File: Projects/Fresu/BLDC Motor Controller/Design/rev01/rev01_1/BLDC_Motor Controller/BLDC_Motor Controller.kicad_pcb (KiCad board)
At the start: 2 copper layers, 65 x 56 mm, 4 parts

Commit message: Update 14
Added 4 mounting holes, imported all components into PCB project, created board outline
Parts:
- removed MH1, MH2, MH3, MH4: MountingHole_2.7mm_M2.5, MountingHole:MountingHole_2.7mm_M2.5
- added C1: C, Capacitor_SMD:C_0603_1608Metric, F.Cu at (444.5, 121.0)
- added C10: 2u2, Capacitor_SMD:C_0603_1608Metric, F.Cu at (448.5, 128.5)
- added C11: 100n, Capacitor_SMD:C_0603_1608Metric, F.Cu at (448.5, 131.0)
- added C12: 1u, Capacitor_SMD:C_0603_1608Metric, F.Cu at (448.5, 133.5)
- added C13: 10p, Capacitor_SMD:C_0603_1608Metric, F.Cu at (452.5, 121.0)
- added C14: 10p, Capacitor_SMD:C_0603_1608Metric, F.Cu at (452.5, 123.5)
- added C15: 100n, Capacitor_SMD:C_0603_1608Metric, F.Cu at (452.5, 126.0)
- added C16: 100n, Capacitor_SMD:C_0603_1608Metric, F.Cu at (452.5, 128.5)
- added C17: 100nF, Capacitor_SMD:C_0603_1608Metric, F.Cu at (452.5, 131.0)
- added C18: 2u2, Capacitor_SMD:C_0603_1608Metric, F.Cu at (497.8, 100.1)
- added C19: 2u2, Capacitor_SMD:C_0603_1608Metric, F.Cu at (497.8, 102.6)
- added C2: 100nF, Capacitor_SMD:C_0603_1608Metric, F.Cu at (444.5, 123.5)
- added C20: 2u2, Capacitor_SMD:C_0603_1608Metric, F.Cu at (497.8, 105.1)
- added C21: 2u2, Capacitor_SMD:C_0603_1608Metric, F.Cu at (497.8, 107.6)
- added C22: 10n, Capacitor_SMD:C_0603_1608Metric, F.Cu at (497.8, 110.1)
- added C23: 120p, Capacitor_SMD:C_0603_1608Metric, F.Cu at (497.8, 112.6)
- added C24: 22n, Capacitor_SMD:C_0603_1608Metric, F.Cu at (501.8, 100.1)
- added C25: 2u2, Capacitor_SMD:C_0603_1608Metric, F.Cu at (501.8, 102.6)
- added C26: 100n, Capacitor_SMD:C_0603_1608Metric, F.Cu at (501.8, 105.1)
- added C27: 100n, Capacitor_SMD:C_0603_1608Metric, F.Cu at (501.8, 107.6)
- added C28: 100n, Capacitor_SMD:C_0603_1608Metric, F.Cu at (501.8, 110.1)
- added C29: 10n, Capacitor_SMD:C_0603_1608Metric, F.Cu at (501.8, 112.6)
- added C3: 100nF, Capacitor_SMD:C_0603_1608Metric, F.Cu at (444.5, 126.0)
- added C30: 10u, Capacitor_SMD:C_0603_1608Metric, F.Cu at (505.8, 100.1)
- added C31: 100n, Capacitor_SMD:C_0603_1608Metric, F.Cu at (505.8, 102.6)
- added C32: 10u, Capacitor_SMD:C_0603_1608Metric, F.Cu at (505.8, 105.1)
- added C33: 10u, Capacitor_SMD:C_0603_1608Metric, F.Cu at (505.8, 107.6)
- added C34: 100n, Capacitor_SMD:C_0603_1608Metric, F.Cu at (505.8, 110.1)
- added C35: 10u, Capacitor_SMD:C_0603_1608Metric, F.Cu at (505.8, 112.6)
- added C36: 10u, Capacitor_SMD:C_0603_1608Metric, F.Cu at (509.8, 100.1)
- added C37: 100n, Capacitor_SMD:C_0603_1608Metric, F.Cu at (509.8, 102.6)
- added C38: 10u, Capacitor_SMD:C_0603_1608Metric, F.Cu at (509.8, 105.1)
- added C39: 10u, Capacitor_SMD:C_0603_1608Metric, F.Cu at (509.8, 107.6)
- added C4: 100nF, Capacitor_SMD:C_0603_1608Metric, F.Cu at (444.5, 128.5)
- added C40: 10u, Capacitor_SMD:C_0603_1608Metric, F.Cu at (509.8, 110.1)
- added C41: 10u, Capacitor_SMD:C_0603_1608Metric, F.Cu at (509.8, 112.6)
- added C42: 2N2, Capacitor_SMD:C_0603_1608Metric, F.Cu at (516.2, 56.3)
- added C43: 2N2, Capacitor_SMD:C_0603_1608Metric, F.Cu at (516.2, 58.8)
- added C44: 100n, Capacitor_SMD:C_0603_1608Metric, F.Cu at (487.1, 78.0)
- added C45: 51p, Capacitor_SMD:C_0603_1608Metric, F.Cu at (515.8, 113.5)
- added C46: 51p, Capacitor_SMD:C_0603_1608Metric, F.Cu at (515.8, 116.0)
- added C47: 2u2, Capacitor_SMD:C_0603_1608Metric, F.Cu at (515.8, 118.5)
- added C48: 4n7, Capacitor_SMD:C_0603_1608Metric, F.Cu at (487.1, 80.5)
- added C49: 4n7, Capacitor_SMD:C_0603_1608Metric, F.Cu at (487.1, 83.0)
- added C5: 100nF, Capacitor_SMD:C_0603_1608Metric, F.Cu at (444.5, 131.0)
- added C50: 100n, Capacitor_SMD:C_0603_1608Metric, F.Cu at (487.1, 85.5)
- added C51: 4n7, Capacitor_SMD:C_0603_1608Metric, F.Cu at (487.1, 88.0)
- added C52: 100n, Capacitor_SMD:C_0603_1608Metric, F.Cu at (487.1, 90.5)
- added C53: 4n7, Capacitor_SMD:C_0603_1608Metric, F.Cu at (487.1, 93.0)
- added C54: 100n, Capacitor_SMD:C_0603_1608Metric, F.Cu at (487.1, 95.6)
- added C55: 1u, Capacitor_SMD:C_0603_1608Metric, F.Cu at (526.3, 34.9)
- added C56: 1u, Capacitor_SMD:C_0603_1608Metric, F.Cu at (526.3, 37.4)
- added C57: 1u, Capacitor_SMD:C_0603_1608Metric, F.Cu at (526.3, 39.9)
- added C58: 1u, Capacitor_SMD:C_0603_1608Metric, F.Cu at (526.3, 42.4)
- added C59: LKMI2501K821MF, DF_ESC_Footprint_Library:CAP-TH_BD18.0-P7.50-D1.2-SIDE, F.Cu at (450.6, 38.5)
- added C6: 100nF, Capacitor_SMD:C_0603_1608Metric, F.Cu at (444.5, 133.5)
- added C61: 100n, Capacitor_SMD:C_0603_1608Metric, F.Cu at (480.3, 79.7)
- added C62: 100n, Capacitor_SMD:C_0603_1608Metric, F.Cu at (480.3, 82.2)
- added C63: LKMI2501K821MF, DF_ESC_Footprint_Library:CAP-TH_BD18.0-P7.50-D1.2-SIDE, F.Cu at (471.0, 38.5)
- added C7: 100nF, Capacitor_SMD:C_0603_1608Metric, F.Cu at (448.5, 121.0)
- added C8: 100nF, Capacitor_SMD:C_0603_1608Metric, F.Cu at (448.5, 123.5)
- added C9: 2u2, Capacitor_SMD:C_0603_1608Metric, F.Cu at (448.5, 126.0)
- added CN1: XT60PW-M, DF_ESC_Footprint_Library:CONN-TH_XT60PW-M, F.Cu at (452.2, 83.5)
- added D1: LED_G, LED_SMD:LED_1206_3216Metric, F.Cu at (472.7, 95.5)
- added D10: BAT60A, Diode_SMD:D_SOD-323, F.Cu at (536.2, 48.4)
- added D11: ESDCAN24-2BLY, Package_TO_SOT_SMD:TSOT-23, F.Cu at (532.0, 120.9)
- added D12: LED_G, LED_SMD:LED_1206_3216Metric, F.Cu at (531.2, 47.0)
- added D13: SMAJ60CA, Diode_SMD:D_SMA, F.Cu at (465.9, 89.4)
- added D14: LED_G, LED_SMD:LED_1206_3216Metric, F.Cu at (476.8, 76.8)
- added D2: LED_R, LED_SMD:LED_1206_3216Metric, F.Cu at (472.7, 98.9)
- added D3: BAT60A, Diode_SMD:D_SOD-323, F.Cu at (477.6, 95.3)
- added D4: BAT60A, Diode_SMD:D_SOD-323, F.Cu at (477.6, 98.3)
- added D5: SD05_SOD323, Diode_SMD:D_SOD-323, F.Cu at (477.6, 101.2)
- added D6: LED_G, LED_SMD:LED_1206_3216Metric, F.Cu at (472.7, 102.3)
- added D7: PMEG6020ELR, Diode_SMD:Nexperia_CFP3_SOD-123W, F.Cu at (498.6, 125.5)
- added D8: BAT60A, Diode_SMD:D_SOD-323, F.Cu at (503.5, 125.4)
- added D9: LED_G, LED_SMD:LED_1206_3216Metric, F.Cu at (531.2, 43.6)
- added FB1: FerriteBead, Inductor_SMD:L_0603_1608Metric_Pad1.05x0.95mm_HandSolder, F.Cu at (471.1, 121.0)
- added FL1: 744227S, DF_ESC_Footprint_Library:FILTER-SMD_4P-L9.2-W6.0-P2.54-TL, F.Cu at (523.9, 116.0)
- added H1: MountingHole_Pad, MountingHole:MountingHole_3.2mm_M3_Pad_Via, F.Cu at (165.4, 104.2)
- added H2: MountingHole_Pad, MountingHole:MountingHole_3.2mm_M3_Pad_Via, F.Cu at (165.4, 169.2)
- added H3: MountingHole_Pad, MountingHole:MountingHole_3.2mm_M3_Pad_Via, F.Cu at (255.4, 104.4)
- added H5: MountingHole_Pad, MountingHole:MountingHole_3.2mm_M3_Pad_Via, F.Cu at (255.2, 169.2)
- added J1: Conn_01x06, DF_ESC_Footprint_Library:CONN-SMD_S6B-XH-SM4-TB-LF-SN, F.Cu at (453.9, 114.1)
- added J10: XH-2PWBPZ, DF_ESC_Footprint_Library:CONN-SMD_XH-2PWBPZ, F.Cu at (467.9, 80.3)
- added J2: Conn_01x03, DF_ESC_Footprint_Library:CONN-SMD_XH-3AWB, F.Cu at (472.1, 111.6)
- added J3: Conn_01x08, DF_ESC_Footprint_Library:CONN-SMD_8P-P2.50_HX25003-8AWB, F.Cu at (456.2, 101.1)
- added J4: 7461084, 7461084:WE_7461084, F.Cu at (499.3, 39.4)
- added J5: 7461084, 7461084:WE_7461084, F.Cu at (499.3, 51.0)
- added J6: 7461084, 7461084:WE_7461084, F.Cu at (499.3, 62.5)
- added J7: TYPE-C-31-M-12, DF_ESC_Footprint_Library:USB-C_SMD-TYPE-C-31-M-12, F.Cu at (528.1, 81.7)
- added J8: Conn_01x06, DF_ESC_Footprint_Library:CONN-SMD_S6B-XH-SM4-TB-LF-SN, F.Cu at (504.9, 84.6)
- added L1: 22u, DF_ESC_Footprint_Library:IND-SMD_L7.8-W7.8_SDR0805, F.Cu at (490.5, 119.2)
- added NT1: NetTie_2, DF_ESC_Footprint_Library:NetTie_SMD_Pad_0.2mm, F.Cu at (507.2, 124.9)
- added NT2: NetTie_2, NetTie:NetTie-2_SMD_Pad0.5mm, F.Cu at (519.4, 55.8)
- added NT3: NetTie_2, DF_ESC_Footprint_Library:NetTie_SMD_Pad_3.00mm, F.Cu at (506.6, 57.6)
- added NT4: NetTie_2, NetTie:NetTie-2_SMD_Pad0.5mm, F.Cu at (519.4, 57.3)
- added NT5: NetTie_2, DF_ESC_Footprint_Library:NetTie_SMD_Pad_3.00mm, F.Cu at (509.6, 57.6)
- added NT6: NetTie_2, NetTie:NetTie-2_SMD_Pad0.5mm, F.Cu at (519.4, 58.8)
- added NT7: NetTie_2, DF_ESC_Footprint_Library:NetTie_SMD_Pad_3.00mm, F.Cu at (512.7, 57.6)
- added Q1: HSBA15810C, Package_DFN_QFN:PQFN-8-EP_6x5mm_P1.27mm_Generic, F.Cu at (489.2, 37.1)
- added Q2: HSBA15810C, Package_DFN_QFN:PQFN-8-EP_6x5mm_P1.27mm_Generic, F.Cu at (489.2, 43.9)
- added Q3: HSBA15810C, Package_DFN_QFN:PQFN-8-EP_6x5mm_P1.27mm_Generic, F.Cu at (489.2, 50.8)
- added Q4: HSBA15810C, Package_DFN_QFN:PQFN-8-EP_6x5mm_P1.27mm_Generic, F.Cu at (489.2, 57.6)
- added Q5: HSBA15810C, Package_DFN_QFN:PQFN-8-EP_6x5mm_P1.27mm_Generic, F.Cu at (489.2, 64.5)
- added Q6: HSBA15810C, Package_DFN_QFN:PQFN-8-EP_6x5mm_P1.27mm_Generic, F.Cu at (489.2, 71.3)
- added R1: 100R, Resistor_SMD:R_0603_1608Metric_Pad0.98x0.95mm_HandSolder, F.Cu at (471.1, 123.5)
- added R10: 2k2, Resistor_SMD:R_0603_1608Metric_Pad0.98x0.95mm_HandSolder, F.Cu at (479.8, 121.0)
- added R11: 16k, Resistor_SMD:R_0603_1608Metric_Pad0.98x0.95mm_HandSolder, F.Cu at (498.0, 115.1)
- added R12: 10k, Resistor_SMD:R_0603_1608Metric_Pad0.98x0.95mm_HandSolder, F.Cu at (498.0, 117.6)
- added R13: 205K, Resistor_SMD:R_0603_1608Metric_Pad0.98x0.95mm_HandSolder, F.Cu at (498.0, 120.2)
- added R14: 1M, Resistor_SMD:R_0603_1608Metric_Pad0.98x0.95mm_HandSolder, F.Cu at (498.0, 122.7)
- added R15: 39k, Resistor_SMD:R_0603_1608Metric_Pad0.98x0.95mm_HandSolder, F.Cu at (502.3, 115.1)
- added R16: 2K2, Resistor_SMD:R_0603_1608Metric_Pad0.98x0.95mm_HandSolder, F.Cu at (502.3, 117.6)
- added R17: 18K, Resistor_SMD:R_0603_1608Metric_Pad0.98x0.95mm_HandSolder, F.Cu at (502.3, 120.2)
- added R18: 3K3, Resistor_SMD:R_0603_1608Metric_Pad0.98x0.95mm_HandSolder, F.Cu at (502.3, 122.7)
- added R19: 39k, Resistor_SMD:R_0603_1608Metric_Pad0.98x0.95mm_HandSolder, F.Cu at (506.7, 115.1)
- added R2: 0R, Resistor_SMD:R_0603_1608Metric_Pad0.98x0.95mm_HandSolder, F.Cu at (471.1, 126.0)
- added R20: 2K2, Resistor_SMD:R_0603_1608Metric_Pad0.98x0.95mm_HandSolder, F.Cu at (506.7, 117.6)
- added R21: 39k, Resistor_SMD:R_0603_1608Metric_Pad0.98x0.95mm_HandSolder, F.Cu at (506.7, 120.2)
- added R22: 2K2, Resistor_SMD:R_0603_1608Metric_Pad0.98x0.95mm_HandSolder, F.Cu at (506.7, 122.7)
- added R23: 4R7, Resistor_SMD:R_0603_1608Metric_Pad0.98x0.95mm_HandSolder, F.Cu at (507.2, 43.7)
- added R24: 4R7, Resistor_SMD:R_0603_1608Metric_Pad0.98x0.95mm_HandSolder, F.Cu at (507.2, 46.2)
- added R25: 39K, Resistor_SMD:R_0603_1608Metric_Pad0.98x0.95mm_HandSolder, F.Cu at (507.2, 48.8)
- added R26: 4R7, Resistor_SMD:R_0603_1608Metric_Pad0.98x0.95mm_HandSolder, F.Cu at (507.2, 51.3)
- added R27: 4R7, Resistor_SMD:R_0603_1608Metric_Pad0.98x0.95mm_HandSolder, F.Cu at (507.2, 53.8)
- added R28: 39K, Resistor_SMD:R_0603_1608Metric_Pad0.98x0.95mm_HandSolder, F.Cu at (511.6, 43.7)
- added R29: 0R001, DF_ESC_Footprint_Library:RES-SMD_L7.0-W6.7, F.Cu at (545.3, 61.8)
- added R29: 0R001, DF_ESC_Footprint_Library:RES-SMD_L7.0-W6.7, F.Cu at (509.4, 38.0)
- added R3: 0R, Resistor_SMD:R_0603_1608Metric_Pad0.98x0.95mm_HandSolder, F.Cu at (471.1, 128.5)
- added R30: 100R, Resistor_SMD:R_0603_1608Metric_Pad0.98x0.95mm_HandSolder, F.Cu at (511.6, 46.2)
- added R31: 100R, Resistor_SMD:R_0603_1608Metric_Pad0.98x0.95mm_HandSolder, F.Cu at (511.6, 48.8)
- added R32: 4R7, Resistor_SMD:R_0603_1608Metric_Pad0.98x0.95mm_HandSolder, F.Cu at (511.6, 51.3)
- added R33: 4R7, Resistor_SMD:R_0603_1608Metric_Pad0.98x0.95mm_HandSolder, F.Cu at (511.6, 53.8)
- added R34: 100R, Resistor_SMD:R_0603_1608Metric_Pad0.98x0.95mm_HandSolder, F.Cu at (515.9, 43.7)
- added R35: 100R, Resistor_SMD:R_0603_1608Metric_Pad0.98x0.95mm_HandSolder, F.Cu at (515.9, 46.2)
- added R36: 39K, Resistor_SMD:R_0603_1608Metric_Pad0.98x0.95mm_HandSolder, F.Cu at (515.9, 48.8)
- added R37: 0R001, DF_ESC_Footprint_Library:RES-SMD_L7.0-W6.7, F.Cu at (518.0, 38.0)
- added R37: 0R, Resistor_SMD:R_0603_1608Metric_Pad0.98x0.95mm_HandSolder, F.Cu at (224.4, 126.7)
- added R38: 2k2, Resistor_SMD:R_0603_1608Metric_Pad0.98x0.95mm_HandSolder, F.Cu at (491.3, 78.0)
- added R39: 10R, Resistor_SMD:R_0603_1608Metric_Pad0.98x0.95mm_HandSolder, F.Cu at (535.6, 100.1)
- added R4: 1k, Resistor_SMD:R_0603_1608Metric_Pad0.98x0.95mm_HandSolder, F.Cu at (471.1, 131.0)
- added R40: 10R, Resistor_SMD:R_0603_1608Metric_Pad0.98x0.95mm_HandSolder, F.Cu at (535.6, 102.6)
- added R41: 120R, Resistor_SMD:R_0603_1608Metric_Pad0.98x0.95mm_HandSolder, F.Cu at (535.6, 105.1)
- added R42: 10K, Resistor_SMD:R_0603_1608Metric_Pad0.98x0.95mm_HandSolder, F.Cu at (535.6, 107.6)
- added R43: 10k, Resistor_SMD:R_0603_1608Metric_Pad0.98x0.95mm_HandSolder, F.Cu at (491.3, 80.5)
- added R44: 2k2, Resistor_SMD:R_0603_1608Metric_Pad0.98x0.95mm_HandSolder, F.Cu at (491.3, 83.0)
- added R45: 10k, Resistor_SMD:R_0603_1608Metric_Pad0.98x0.95mm_HandSolder, F.Cu at (491.3, 85.5)
- added R46: 2k2, Resistor_SMD:R_0603_1608Metric_Pad0.98x0.95mm_HandSolder, F.Cu at (491.3, 88.0)
- added R47: 10k, Resistor_SMD:R_0603_1608Metric_Pad0.98x0.95mm_HandSolder, F.Cu at (491.3, 90.5)
- added R48: 10k, Resistor_SMD:R_0603_1608Metric_Pad0.98x0.95mm_HandSolder, F.Cu at (491.3, 93.0)
- added R49: 0R, Resistor_SMD:R_0603_1608Metric_Pad0.98x0.95mm_HandSolder, F.Cu at (491.3, 95.6)
- added R5: 1k, Resistor_SMD:R_0603_1608Metric_Pad0.98x0.95mm_HandSolder, F.Cu at (475.5, 121.0)
- added R50: 1k, Resistor_SMD:R_0603_1608Metric_Pad0.98x0.95mm_HandSolder, F.Cu at (536.2, 43.1)
- added R51: 1k, Resistor_SMD:R_0603_1608Metric_Pad0.98x0.95mm_HandSolder, F.Cu at (536.2, 45.6)
- added R52: 39k, Resistor_SMD:R_0603_1608Metric_Pad0.98x0.95mm_HandSolder, F.Cu at (476.1, 79.7)
- added R53: 2k2, Resistor_SMD:R_0603_1608Metric_Pad0.98x0.95mm_HandSolder, F.Cu at (476.1, 82.2)
- added R54: 39k, Resistor_SMD:R_0603_1608Metric_Pad0.98x0.95mm_HandSolder, F.Cu at (476.1, 84.8)
- added R55: 2k2, Resistor_SMD:R_0603_1608Metric_Pad0.98x0.95mm_HandSolder, F.Cu at (476.1, 87.3)
- added R56: 2k2, Resistor_SMD:R_0603_1608Metric_Pad0.98x0.95mm_HandSolder, F.Cu at (479.8, 123.5)
- added R57: 0R, Resistor_SMD:R_0603_1608Metric_Pad0.98x0.95mm_HandSolder, F.Cu at (520.5, 78.0)
- added R58: 0R, Resistor_SMD:R_0603_1608Metric_Pad0.98x0.95mm_HandSolder, F.Cu at (520.5, 80.5)
- added R59: 22R, Resistor_SMD:R_0603_1608Metric_Pad0.98x0.95mm_HandSolder, F.Cu at (520.5, 83.0)
- added R6: 1k, Resistor_SMD:R_0603_1608Metric_Pad0.98x0.95mm_HandSolder, F.Cu at (475.5, 123.5)
- added R60: 22R, Resistor_SMD:R_0603_1608Metric_Pad0.98x0.95mm_HandSolder, F.Cu at (520.5, 85.5)
- added R61: 5K1, Resistor_SMD:R_0603_1608Metric_Pad0.98x0.95mm_HandSolder, F.Cu at (520.5, 88.0)
- added R62: 5K1, Resistor_SMD:R_0603_1608Metric_Pad0.98x0.95mm_HandSolder, F.Cu at (520.5, 90.5)
- added R63: 0R, Resistor_SMD:R_0603_1608Metric_Pad0.98x0.95mm_HandSolder, F.Cu at (520.5, 93.0)
- added R64: 0R001, DF_ESC_Footprint_Library:RES-SMD_L7.0-W6.7, F.Cu at (553.9, 61.8)
- added R65: 0R, Resistor_SMD:R_0603_1608Metric_Pad0.98x0.95mm_HandSolder, F.Cu at (224.4, 129.2)
- added R66: 0R, Resistor_SMD:R_0603_1608Metric_Pad0.98x0.95mm_HandSolder, F.Cu at (224.4, 131.7)
- added R67: 0R, Resistor_SMD:R_0603_1608Metric_Pad0.98x0.95mm_HandSolder, F.Cu at (224.4, 134.2)
- added R7: 2k2, Resistor_SMD:R_0603_1608Metric_Pad0.98x0.95mm_HandSolder, F.Cu at (475.5, 126.0)
- added R8: 2k2, Resistor_SMD:R_0603_1608Metric_Pad0.98x0.95mm_HandSolder, F.Cu at (475.5, 128.5)
- added R9: 39k, Resistor_SMD:R_0603_1608Metric_Pad0.98x0.95mm_HandSolder, F.Cu at (475.5, 131.0)
- added SW2: PTS526SK15SMTR2LFS, DF_ESC_Footprint_Library:SW-SMD_4P-L5.2-W5.2-P3.70-LS6.4, F.Cu at (473.5, 135.8)
- added TH1: 10K, Resistor_SMD:R_0603_1608Metric_Pad0.98x0.95mm_HandSolder, F.Cu at (479.8, 126.0)
- added TH2: 10k, Resistor_SMD:R_0603_1608Metric_Pad0.98x0.95mm_HandSolder, F.Cu at (476.1, 89.8)
- added U1: STM32F405RGTx, Package_QFP:LQFP-64_10x10mm_P0.5mm, F.Cu at (461.7, 127.0)
- added U2: DRV8302_DCA_56, Package_SO:HTSSOP-56-1EP_6.1x14mm_P0.5mm_EP3.61x6.35mm, F.Cu at (490.5, 106.6)
- added U3: SN65HVD230, Package_SO:SOIC-8_3.9x4.9mm_P1.27mm, F.Cu at (533.5, 115.5)
- added U4: AMS1117-3.3, Package_TO_SOT_SMD:SOT-223-3_TabPin2, F.Cu at (533.3, 37.8)
- added U5: S4B-XH-SM4-TB-(LF)(SN), DF_ESC_Footprint_Library:CONN-SMD_S4B-XH-SM4-TB-LF-SN, F.Cu at (523.6, 107.0)
- added U6: PUSB3AB6Z, DF_ESC_Footprint_Library:XSON-7_L2.2-W1.2-P0.50-BL, F.Cu at (524.6, 87.4)
- added Y1: 8MHz, DF_ESC_Footprint_Library:CRYSTAL-SMD_L5.0-W3.2, F.Cu at (458.5, 136.7)
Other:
- board size 65 x 56 mm -> 100 x 75 mm

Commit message: Update 15
Fixing some schematic errors

initial layout of larger component complete
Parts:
- removed the R37 at (518.0, 38.0)
- added D15: BAT60A, Diode_SMD:D_SOD-323, F.Cu at (194.9, 179.3)
- C56: renamed from C63; moved to B.Cu
- C57: renamed from C59; moved to B.Cu
- moved R29 544.5 mm to (3.83, 3.83)
- moved R42 384.7 mm to (151.1, 118.3)
- moved C46 382.7 mm to (133.3, 127.2)
- moved R39 358.5 mm to (177.4, 118.4), turned to -90 degrees
- moved U3 358.4 mm to (165.4, 118.3), turned to -90 degrees
- moved D9 357.0 mm to (174.9, 118.4)
- moved R40 356.4 mm to (179.8, 120.6)
- moved R41 356.0 mm to (179.9, 118.1)
- moved C44 339.5 mm to (176.4, 120.9), turned to 180 degrees
- moved C45 339.5 mm to (176.4, 115.8), turned to 180 degrees
- moved FL1 337.2 mm to (186.8, 119.1)
- moved C1 336.2 mm to (111.6, 167.9)
- moved C10 336.2 mm to (115.6, 172.9)
- moved C11 336.2 mm to (115.6, 170.4)
- moved C13 336.2 mm to (115.6, 175.4)
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- renumbered C9 to C10, C8 to C11, C17 to C12, C10 to C13, C11 to C14, C12 to C15, C15 to C16, C16 to C17, C43 to C42, C42 to C43, C45 to C44, C46 to C45, C47 to C46, C48 to C47, C49 to C48, C51 to C49, C53 to C50, C44 to C51, C50 to C52, C52 to C53, C62 to C55, C61 to C58, C56 to C59, C55 to C60, C57 to C61, C58 to C62, C13 to C8, C14 to C9, D6 to D1, D13 to D10, D14 to D11, D9 to D12, D10 to D13, D12 to D14, D5 to D2, D1 to D5, D2 to D6, D11 to D9, H3 to H1, H5 to H2, H2 to H3, H1 to H4, J3 to J1, J1 to J2, J2 to J3, J8 to J7, J10 to J8, J7 to J9, NT6 to NT2, NT7 to NT3, NT2 to NT6, NT3 to NT7, Q5 to Q1, Q6 to Q2, Q1 to Q5, Q2 to Q6, R6 to R1, R7 to R10, R8 to R11, R11 to R12, R12 to R13, R13 to R14, R14 to R15, R15 to R16, R16 to R17, R17 to R18, R18 to R19, R4 to R2, R19 to R20, R20 to R21, R21 to R22, R22 to R23, R32 to R24, R33 to R25, R34 to R26, R35 to R27, R36 to R28, R56 to R3, R26 to R30, R27 to R31, R30 to R32, R31 to R33, R28 to R34, R64 to R35, R23 to R36, R24 to R37, R25 to R38, R41 to R39, R5 to R4, R39 to R40, R40 to R41, R38 to R43, R46 to R45, R48 to R46, R43 to R47, R45 to R48, R47 to R49, R2 to R5, R49 to R50, R67 to R51, R37 to R52, R66 to R53, R65 to R54, R52 to R56, R53 to R57, R54 to R58, R50 to R59, R3 to R6, R51 to R60, R57 to R61, R58 to R62, R61 to R64, R62 to R65, R60 to R66, R59 to R67, R9 to R7, R10 to R8, R1 to R9, SW2 to SW1, U5 to U3, U3 to U4, U4 to U5
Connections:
- net /MCU/MISO_ADC_EXT renamed /MCU/MISO_ADC_EXT2
- D2 pad 1: unconnected-(D5-A1-Pad1) -> GND
- D2 pad 2: unconnected-(D5-A2-Pad2) -> Net-(D2-A2)
- D3 pad 1: unconnected-(D3-K-Pad1) -> +5V
- D3 pad 2: unconnected-(D3-A-Pad2) -> Net-(D2-A2)
- D4 pad 1: unconnected-(D4-K-Pad1) -> +3V3
- D4 pad 2: unconnected-(D4-A-Pad2) -> Net-(D4-A)
- J1 pad 1: +5V -> Net-(D2-A2)
- J1 pad 2: unconnected-(J3-Pin_2-Pad2) -> Net-(D4-A)
- J1 pad 3: unconnected-(J3-Pin_3-Pad3) -> GND
- J2 pad 1: +3V3 -> Net-(D15-A)
- J2 pad 2: /MCU/SWCLK -> /MCU/SWDIO
- J2 pad 4: /MCU/SWDIO -> /MCU/SWCLK
- J2 pad 5: /MCU/NRST -> GND
- J2 pad 6: unconnected-(J1-Pin_6-Pad6) -> /MCU/NRST
- U1 pad 1: unconnected-(U1-VBAT-Pad1) -> +3V3
- U1 pad 14: SENS1 -> SENS3
- U1 pad 20: /MCU/TX_SDA_NSS -> /MCU/RX_SDA_NSS
- U1 pad 23: /MCU/RX_SCI_MOSI -> /MCU/TX_SCI_MOSI
- U1 pad 26: /MCU/BR_S02 -> BR_S02
- U1 pad 27: /MCU/BR_S01 -> BR_S01
- U1 pad 33: /MCU/DC_CAL -> DC_CAL
- U1 pad 34: /MCU/L3 -> L3
- U1 pad 35: /MCU/L2 -> L2
- U1 pad 36: /MCU/L1 -> L1
- U1 pad 41: /MCU/H3 -> H3
- U1 pad 42: /MCU/H2 -> H2
- U1 pad 43: /MCU/H1 -> H1
- U1 pad 44: /MCU/USB_DM -> USB_N
- U1 pad 45: /MCU/USB_DP -> USB_P
- U1 pad 51: /MCU/EN_GATE -> EN_GATE
- U1 pad 53: /MCU/FAULT -> FAULT
- U1 pad 61: /MCU/CAN_RX -> CAN_RX
- U1 pad 62: /MCU/CAN_TX -> CAN_TX
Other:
- copper layers 2 -> 4

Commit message: Update 16
Almost finished placing all the components on the board as rough placement
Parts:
- removed C12: 100nF, Capacitor_SMD:C_0603_1608Metric
- removed C17: 100n, Capacitor_SMD:C_0603_1608Metric
- removed D1: LED_G, LED_SMD:LED_1206_3216Metric
- removed R1: 1k, Resistor_SMD:R_0603_1608Metric_Pad0.98x0.95mm_HandSolder
- removed R11, R8: 2k2, Resistor_SMD:R_0603_1608Metric_Pad0.98x0.95mm_HandSolder
- removed the R29 at (3.83, 3.83)
- removed the R29 at (233.5, 132.7)
- removed R7: 39k, Resistor_SMD:R_0603_1608Metric_Pad0.98x0.95mm_HandSolder
- removed TH1: 10K, Resistor_SMD:R_0603_1608Metric_Pad0.98x0.95mm_HandSolder
- added NT8: Net_Tie_PWR, DF_ESC_Footprint_Library:NetTie_SMD_Pad_6.00mm, F.Cu at (229.7, 131.8)
- added NT9: Net_Tie_PWR, DF_ESC_Footprint_Library:NetTie_SMD_Pad_6.00mm, F.Cu at (229.8, 146.4)
- added R29: 0R001, DF_ESC_Footprint_Library:RES-SMD_L7.0-W6.7, F.Cu at (235.5, 132.5)
- C1: value C -> 10u
- C22, C23, C24, C31, C34, C37, C58, D10, NT2, NT4, NT6, R12, R26, R27, R32, R33: moved to B.Cu
- C29: value 10n -> 100n
- C30, C32, C33, C35, C36, C38: value 10u -> 1u
- C39, C40, C41: footprint Capacitor_SMD:C_0603_1608Metric -> Capacitor_SMD:C_1206_3216Metric
- C42, C43: value 2N2 -> 2n2; moved to B.Cu
- NT7: value NetTie_2 -> Net_Tie_PWR; footprint DF_ESC_Footprint_Library:NetTie_SMD_Pad_3.00mm -> DF_ESC_Footprint_Library:NetTie_SMD_Pad_6.00mm
- Q1, Q2, Q3, Q4, Q5, Q6: footprint Package_DFN_QFN:PQFN-8-EP_6x5mm_P1.27mm_Generic -> DF_ESC_Footprint_Library:PQFN-8_L6.0-W5.0-P1.27-LS6.0-BL
- moved NT2 128.8 mm to (223.6, 141.9)
- moved NT4 128.1 mm to (223.6, 143.0)
- moved NT6 127.5 mm to (223.6, 144.0)
- moved C55 126.7 mm to (177.9, 156.5)
- moved C43 124.2 mm to (221.9, 152.4), turned to -90 degrees
- moved C42 123.2 mm to (223.4, 152.6), turned to -90 degrees
- moved R26 119.6 mm to (224.8, 149.3), turned to 180 degrees
- moved R27 119.6 mm to (224.8, 151.8), turned to 180 degrees
- moved R16 119.1 mm to (151.7, 151.4)
- moved R17 118.7 mm to (152.0, 154.1)
- moved R20 118.7 mm to (156.3, 151.6)
- moved R21 118.7 mm to (156.3, 154.1)
- moved R23 118.7 mm to (156.3, 159.2)
- moved R22 118.7 mm to (156.3, 156.6)
- moved D8 117.7 mm to (207.1, 124.9)
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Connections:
- J7 pad 1: +5V -> GND
- J7 pad 2: /Filters/TEMP_IN -> /Filters/HALL_3_IN
- J7 pad 3: /Filters/HALL_1_IN -> /Filters/HALL_2_IN
- J7 pad 4: /Filters/HALL_2_IN -> /Filters/HALL_1_IN
- J7 pad 5: /Filters/HALL_3_IN -> /Filters/TEMP_IN
- J7 pad 6: GND -> +5V
- J9 pad A5: Net-(J9-CC1) -> /USB/CC1
- J9 pad B5: Net-(J9-CC2) -> /USB/CC2
- Q1 pad 1: +VDC -> /MOSFETS/PHASE_1
- Q1 pad 2: /MOSFETS/M_H1_RG -> /MOSFETS/PHASE_1
- Q1 pad 4: (no net) -> /MOSFETS/M_H1_RG
- Q1 pad 5: (no net) -> +VDC
- Q2 pad 1: /MOSFETS/PHASE_1 -> H1_LOW
- Q2 pad 2: /MOSFETS/M_L1_RG -> H1_LOW
- Q2 pad 4: (no net) -> /MOSFETS/M_L1_RG
- Q2 pad 5: (no net) -> /MOSFETS/PHASE_1
- Q3 pad 1: +VDC -> /MOSFETS/PHASE_2
- Q3 pad 2: /MOSFETS/M_H2_RG -> /MOSFETS/PHASE_2
- Q3 pad 4: (no net) -> /MOSFETS/M_H2_RG
- Q3 pad 5: (no net) -> +VDC
- Q4 pad 1: /MOSFETS/PHASE_2 -> H2_LOW
- Q4 pad 2: /MOSFETS/M_L2_RG -> H2_LOW
- Q4 pad 4: (no net) -> /MOSFETS/M_L2_RG
- Q4 pad 5: (no net) -> /MOSFETS/PHASE_2
- Q5 pad 1: +VDC -> /MOSFETS/PHASE_3
- Q5 pad 2: /MOSFETS/M_H3_RG -> /MOSFETS/PHASE_3
- Q5 pad 4: (no net) -> /MOSFETS/M_H3_RG
- Q5 pad 5: (no net) -> +VDC
- Q6 pad 1: /MOSFETS/PHASE_3 -> H3_LOW
- Q6 pad 2: /MOSFETS/M_L3_RG -> H3_LOW
- Q6 pad 4: (no net) -> /MOSFETS/M_L3_RG
- Q6 pad 5: (no net) -> /MOSFETS/PHASE_3
- R18 pad 1: /FET Driver/V_SENSE -> /FET Driver/VSENSE
- R19 pad 2: /FET Driver/V_SENSE -> /FET Driver/VSENSE
- R27 pad 2: GND -> /MOSFETS/SH1_P
- R33 pad 2: GND -> /MOSFETS/SH2_P
- R35 pad 1: /MOSFETS/SH2_N -> /MOSFETS/SH2_P
- R35 pad 2: GND -> /MOSFETS/SH2_N
- R64 pad 1: Net-(J9-CC2) -> /USB/CC2
- R65 pad 1: Net-(J9-CC1) -> /USB/CC1
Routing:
- net DC_CAL: track 0.00 -> 11.0 mm

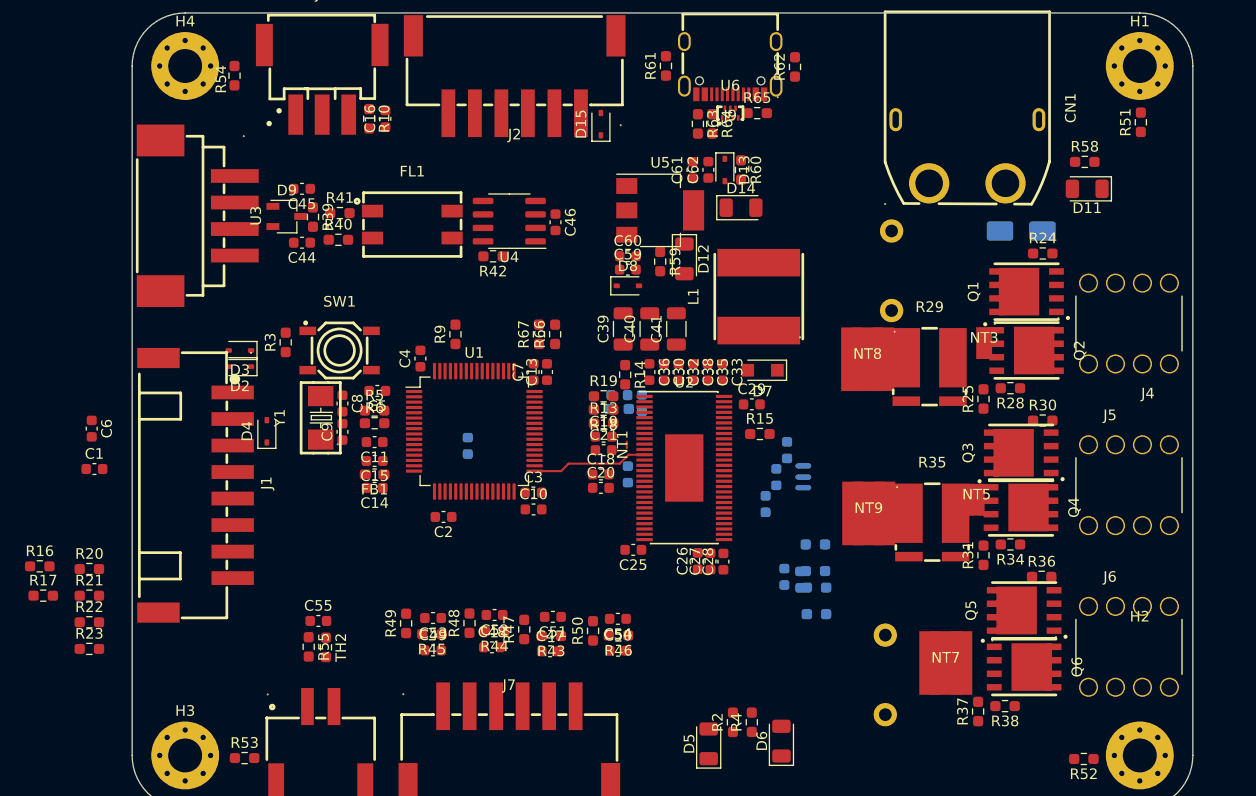
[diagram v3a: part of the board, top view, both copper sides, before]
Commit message: Update 17
Started laying out the driver and the main FET power polygons
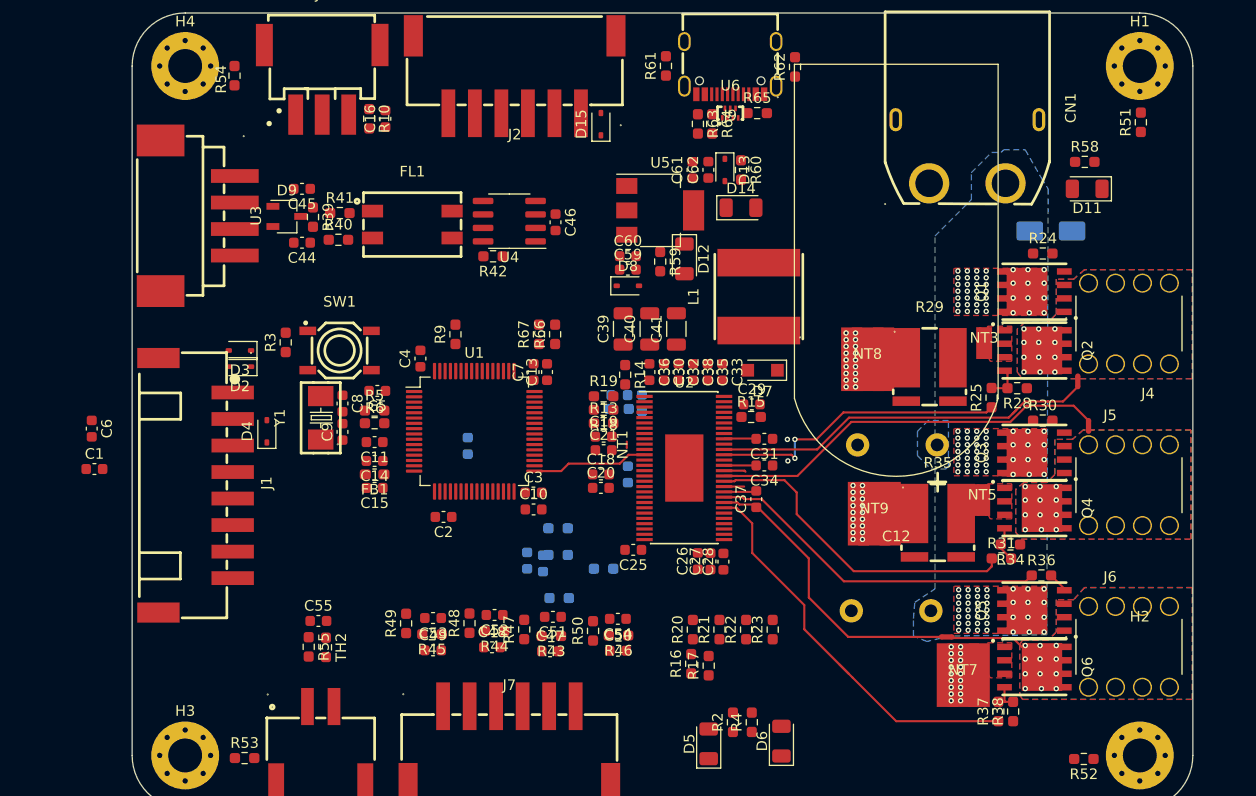
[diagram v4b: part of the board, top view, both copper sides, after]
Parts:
- removed C56: LKMI2501K821MF, DF_ESC_Footprint_Library:CAP-TH_BD18.0-P7.50-D1.2-SIDE
- added C12: LKMI2501K821MF, DF_ESC_Footprint_Library:CAP-TH_BD18.0-P7.50-D1.2-SIDE, F.Cu at (234.4, 140.0)
- C31, C34, C37, NT2, NT4, NT6: moved to F.Cu
- moved R23 64.4 mm to (220.8, 157.3), turned to 90 degrees
- moved R17 63.1 mm to (214.7, 160.7), turned to 90 degrees
- moved R16 62.1 mm to (213.1, 160.6), turned to 90 degrees
- moved R22 61.9 mm to (218.2, 157.3), turned to 90 degrees
- moved R21 59.5 mm to (215.7, 157.3), turned to 90 degrees
- moved R20 57.2 mm to (213.2, 157.3), turned to 90 degrees
- moved NT4 27.3 mm to (250.5, 138.1), turned to -90 degrees
- moved NT2 27.1 mm to (249.5, 133.9), turned to 90 degrees
- moved C42 24.3 mm to (199.1, 151.1)
- moved C43 24.3 mm to (197.6, 150.8)
- moved R26 24.3 mm to (200.5, 147.8)
- moved R27 24.3 mm to (200.5, 150.3)
- moved R33 24.3 mm to (200.6, 154.4)
- moved R32 20.1 mm to (204.8, 151.6)
- moved NT6 19.5 mm to (237.2, 158.0)
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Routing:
- net H2_VS: track 0.00 -> 39.0 mm
- net M_L3: track 0.00 -> 38.4 mm
- net H1_VS: track 0.00 -> 36.3 mm
- net M_H3: track 0.00 -> 32.5 mm
- net M_L2: track 0.00 -> 31.0 mm
- net M_L1: track 0.00 -> 28.6 mm, vias 0 -> 2
- net H3_VS: track 0.00 -> 27.9 mm
- net /MOSFETS/PHASE_3: track 0.00 -> 9.73 mm, vias 0 -> 12
- net /MOSFETS/M_L2_RG: track 0.00 -> 3.40 mm
- net /MOSFETS/M_L1_RG: track 0.00 -> 3.28 mm
- net /FET Driver/BST_C: track 0.00 -> 3.06 mm
- net /FET Driver/BST_B: track 0.00 -> 2.95 mm
- net /FET Driver/BST_A: track 0.00 -> 2.95 mm
- net /MOSFETS/M_L3_RG: track 0.00 -> 2.79 mm
- net M_H2: track 0.00 -> 2.06 mm
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- added copper zone on B.Cu, net +VDC
- added copper zone on F.Cu, net +VDC
- added copper zone on B.Cu, net /MOSFETS/PHASE_1
- added copper zone on F.Cu, net /MOSFETS/PHASE_1
- added copper zone on B.Cu, net /MOSFETS/PHASE_2
- added copper zone on F.Cu, net /MOSFETS/PHASE_2
- added copper zone on B.Cu, net /MOSFETS/PHASE_3
- added copper zone on F.Cu, net /MOSFETS/PHASE_3
- added copper zone on In1.Cu, net GND
- added copper zone on In2.Cu, net GND
- added copper zone on F.Cu, net H1_LOW
- added copper zone on F.Cu, net H3_LOW

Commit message: Update 18
almost done routing driver chip and MCU (first pass)
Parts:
- added C56: LKMI2501K821MF, DF_ESC_Footprint_Library:CAP-TH_BD18.0-P7.50-D1.2-SIDE, F.Cu at (7.67, 4.39)
- moved C43 22.2 mm to (219.7, 148.8)
- moved R27 21.9 mm to (222.1, 146.8), turned to 0 degrees
- moved R33 21.9 mm to (222.0, 149.7), turned to 0 degrees
- moved R26 21.7 mm to (222.1, 145.4), turned to 0 degrees
- moved C42 21.3 mm to (219.8, 146.1)
- moved R32 17.5 mm to (222.0, 148.3), turned to 0 degrees
- moved NT4 14.7 mm to (236.6, 142.9), turned to 0 degrees
- moved NT2 14.2 mm to (236.6, 128.1), turned to 0 degrees
- moved R23 3.96 mm to (216.8, 157.2)
- moved C24 3.60 mm to (210.6, 141.7)
- moved C34 3.30 mm to (223.1, 142.7), turned to 45 degrees
- moved R66 3.10 mm to (203.3, 129.8)
- moved R67 3.10 mm to (201.8, 129.8)
- moved C55 2.57 mm to (178.9, 158.9)
- moved C31 2.54 mm to (222.5, 139.3), turned to 90 degrees
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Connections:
- U1 pad 23: /MCU/TX_SCI_MOSI -> /MCU/TX_SCL_MOSI
- U1 pad 29: /MCU/TX_SCI_MOSI -> /MCU/TX_SCL_MOSI
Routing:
- net H3_LOW: track 0.00 -> 44.4 mm
- net M_H1: track 0.00 -> 43.3 mm
- net /MCU/TX_SCL_MOSI: track 0.00 -> 41.1 mm, vias 0 -> 2
- net /MCU/RX_SDA_NSS: track 0.00 -> 39.8 mm, vias 0 -> 2
- net /MCU/SCK_ADC_EXT: track 0.00 -> 38.5 mm
- net H1_LOW: track 0.00 -> 35.4 mm
- net H2_LOW: track 1.89 -> 35.8 mm
- net M_H2: track 2.06 -> 33.3 mm
- net /MCU/LED_GREEN: track 0.00 -> 31.1 mm
- net /MCU/LED_RED: track 0.00 -> 31.0 mm
- net /MCU/MISO_ADC_EXT2: track 0.00 -> 29.5 mm
- net +3V3: track 0.00 -> 29.0 mm
- net /MOSFETS/SH1_N: track 0.00 -> 25.6 mm, vias 0 -> 1
- net /MOSFETS/SH1_P: track 0.00 -> 25.2 mm, vias 0 -> 1
- net ADC_TEMP: track 0.00 -> 21.7 mm, vias 0 -> 2
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- added copper zone on F.Cu, net /FET Driver/+5V_DRV
- added copper zone on F.Cu, net /FET Driver/PH
- added copper zone on F.Cu, net GND
- added copper zone on F.Cu, net H2_LOW

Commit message: Update 19
further MCU layout
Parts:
- moved NT1 0.59 mm to (206.6, 139.7), turned to -90 degrees
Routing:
- net +3V3: track 29.0 -> 14.9 mm
- net GND: track 17.5 -> 27.5 mm, vias 92 -> 103
- net /FET Driver/DVDD: track 0.00 -> 9.64 mm, vias 0 -> 2
- net /MCU/SWDIO: track 2.71 -> 9.14 mm
- net USB_N: track 3.94 -> 9.40 mm
- net USB_P: track 3.36 -> 8.64 mm
- net /FET Driver/OC_ADJ: track 0.00 -> 4.78 mm
- net /MCU/MISO_ADC_EXT2: track 29.5 -> 26.8 mm
- net /MCU/VCAP_2: track 0.00 -> 2.53 mm
- net /FET Driver/RT_CLK: track 0.00 -> 2.29 mm
- net /FET Driver/CP1: track 0.00 -> 2.28 mm, vias 0 -> 1
- net /FET Driver/CP2: track 0.00 -> 2.03 mm, vias 0 -> 1
- net H2: track 13.4 -> 15.0 mm
- net L1: track 12.0 -> 13.4 mm
- net EN_GATE: track 18.2 -> 19.2 mm
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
